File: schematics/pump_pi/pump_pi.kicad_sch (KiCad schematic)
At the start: 0 parts

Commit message: update schematics
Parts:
- added J1: Raspberry_Pi_4, symbol Connector:Raspberry_Pi_4
- added R1: 330, symbol Device:R
- added R2, R3, R4: 10k, symbol Device:R
- added RV1: R_Potentiometer, symbol Device:R_Potentiometer
- added SW1, SW2, SW3: SW_Push, symbol Switch:SW_Push
- added SW4: SW_Wuerth_450301014042, Button_Switch_THT:SW_Slide-03_Wuerth-WS-SLTV_10x2.5x6.4_P2.54mm, symbol Switch:SW_Wuerth_450301014042
- added U1: MCP3008, symbol Analog_ADC:MCP3008
- added U2: TLP3542, Package_DIP:DIP-5-6_W7.62mm, symbol Relay_SolidState:TLP3542
- added U3: Vacuum sensor, symbol shm_symbols:Vacuum_sensor
- added U4: Voltage meter, symbol shm_symbols:Voltage_meter
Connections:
- new net: SW4.1 (B), U1.1 (CH0), U4. (Black)
- new net: RV1.2, SW4.2 (C)
- new net: SW4.3 (A), U3. (Black)
- new net: R1.1, U2.1
- new net: J1.14 (GND), J1.20 (GND), J1.25 (GND), J1.30 (GND), J1.34 (GND), J1.39 (GND), J1.6 (GND), J1.9 (GND), R2.1, R3.1, R4.1, RV1.1, U1.14 (AGND), U1.9 (DGND), U2.2, U3. (Black), U4. (Black)
- new net: J1.1 (3V3), J1.17 (3V3)
- new net: J1.15 (GPIO22/SDIO_CLK), R1.2
- new net: J1.19 (MOSI_SPI0/GPIO10), U1.11 (Din)
- new net: J1.2 (5V), J1.4 (5V), RV1.3, SW1.2, SW2.2, SW3.2, U1.15 (Vref), U1.16 (Vdd), U3. (Black), U4. (Black)
- new net: J1.21 (MISO_SPI0/GPIO09), U1.12 (Dout)
- new net: J1.23 (SCLK_SPI0/GPIO11), U1.13 (CLK)
- new net: J1.29 (GPCLK1/GPIO05), U1.10 (~{CS}/SHDN)
- new net: R4.2, SW3.1, U1.4 (CH3)
- new net: R2.2, SW1.1, U1.2 (CH1)
- new net: R3.2, SW2.1, U1.3 (CH2)
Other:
- note added: "Auto pump on"
- note added: "Manual pump on"
- note added: "Tank empty pump off"

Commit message: update schematics
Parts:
- removed RV1: R_Potentiometer, symbol Device:R_Potentiometer
- removed SW4: SW_Wuerth_450301014042, Button_Switch_THT:SW_Slide-03_Wuerth-WS-SLTV_10x2.5x6.4_P2.54mm, symbol Switch:SW_Wuerth_450301014042
- added R10, R11, R9: 10k, symbol Device:R
- added SW10, SW11, SW9: SW_Push, symbol Switch:SW_Push
- added U9: Pump control chip, symbol shm_symbols:Pump_control_chip
- SW1, SW3: value SW_Push -> Float
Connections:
- net at U1.1 (CH0), U4. (Black): now also U3. (Black)
- net at J1.14 (GND), J1.20 (GND), J1.25 (GND)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: now also R10.1, R11.1, R9.1, U9. (GND)
- net at U2.4: now also U9. (GND)
- net at U2.6: now also J1.2 (5V), J1.4 (5V), SW1.2, SW2.2, SW3.2, U1.15 (Vref), U1.16 (Vdd), U3. (Black), U4. (Black), SW10.2, SW11.2, SW9.2
- net at U1.6 (CH5): now also R9.2, SW9.1
- net at U1.7 (CH6): now also R10.2, SW10.1
- net at U1.8 (CH7): now also R11.2, SW11.1
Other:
- note added: "Controller off"
- note added: "Reset error"
- note added: "controller on"
- moved on the sheet: J1, R1, R2, R3, R4, SW1, SW2, SW3, U1, U2, U3, U4

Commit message: update schematics
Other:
- moved on the sheet: R10, R11, R2, R3, R4, R9, SW1, SW10, SW11, SW2, SW3, SW9

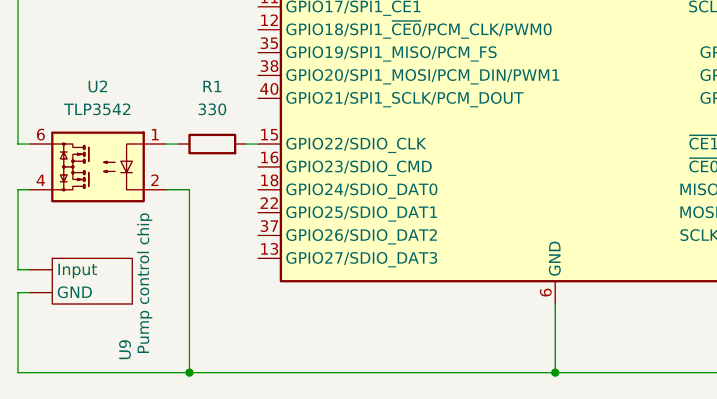
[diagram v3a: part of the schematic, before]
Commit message: Update schematics and figures
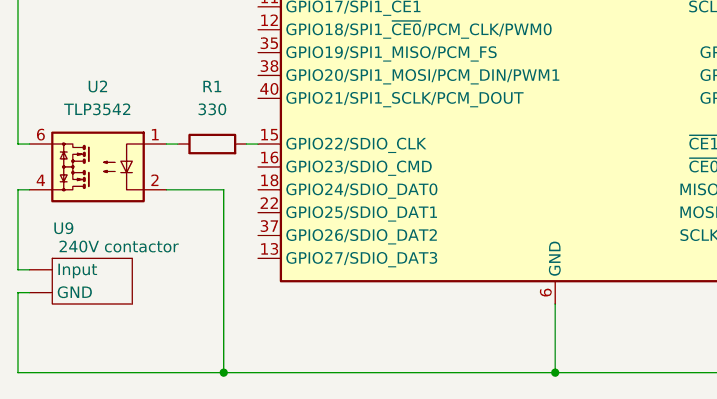
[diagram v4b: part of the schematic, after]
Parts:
- U9: value Pump control chip -> 240V contactor
